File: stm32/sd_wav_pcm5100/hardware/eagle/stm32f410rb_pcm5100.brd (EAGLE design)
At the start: 46.1 x 58.2 mm, 33 parts, among them IC1 STM32F410_8_B_LQFP64, U5 ROBERTSONICS_PCM5100

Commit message: added shenzen2u/smart-proto cam/dru files
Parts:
- IC1: value STM32F410_8_B_LQFP64 -> STM32F410
- U5: value ROBERTSONICS_PCM5100 -> PCM5100
- moved R4 0.36 mm to (7.62, 22.2)

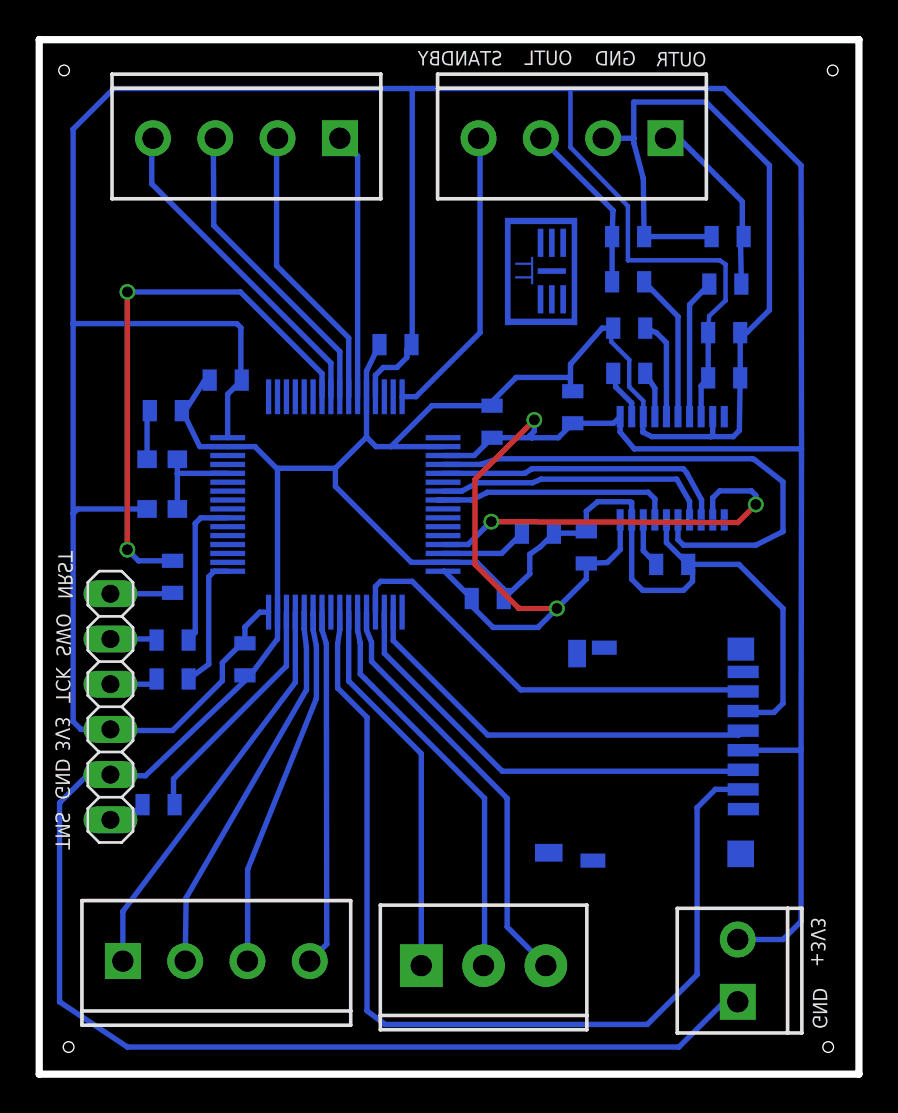
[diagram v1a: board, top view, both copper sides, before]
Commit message: added 3d renderings
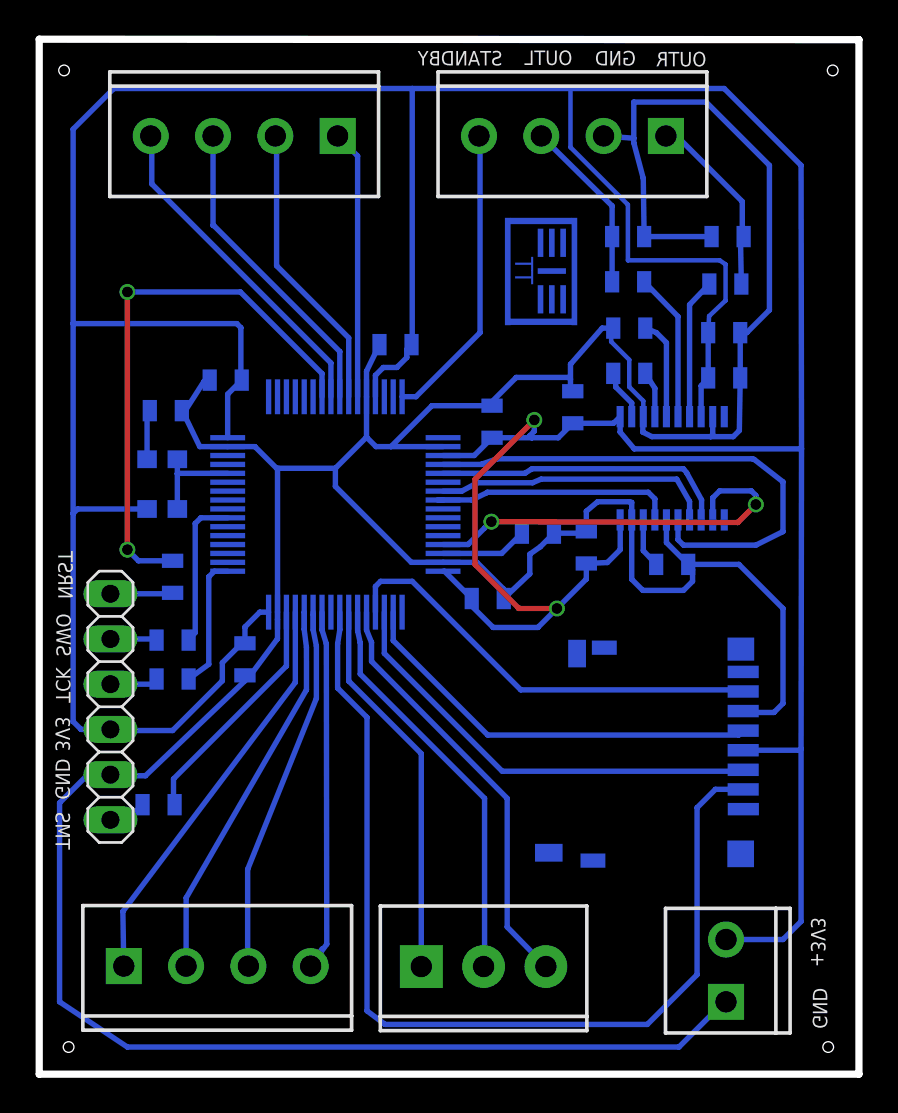
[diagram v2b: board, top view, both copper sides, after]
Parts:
- moved JP3 5.46 mm to (11.6, 52.7)
- moved JP7 5.39 mm to (10.2, 6.07)
- moved JP6 5.31 mm to (30.0, 52.7)
- moved JP5 3.56 mm to (25.1, 6.05)
- moved JP2 1.90 mm to (38.7, 5.84)
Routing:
- net VCC: track 261.5 -> 262.2 mm
- net GND: track 221.4 -> 220.8 mm
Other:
- outline, holes or cut-outs redrawn
